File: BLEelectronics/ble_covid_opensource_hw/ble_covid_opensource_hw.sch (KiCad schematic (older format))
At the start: 35 parts, among them IC1 LTC4412xS6, IC2 LTC4054LES5-4.2#TRPBF, IC3 PCF8523T, IC4 MX25R6435FM2IL0, J1 USB_B_Micro, J2 Conn_01x01_Female, Q1 Si2307CDS, U1 BAT-HLD-001, U2 ESD401, U3 ESD401, U4 LP5907MFX-3.3

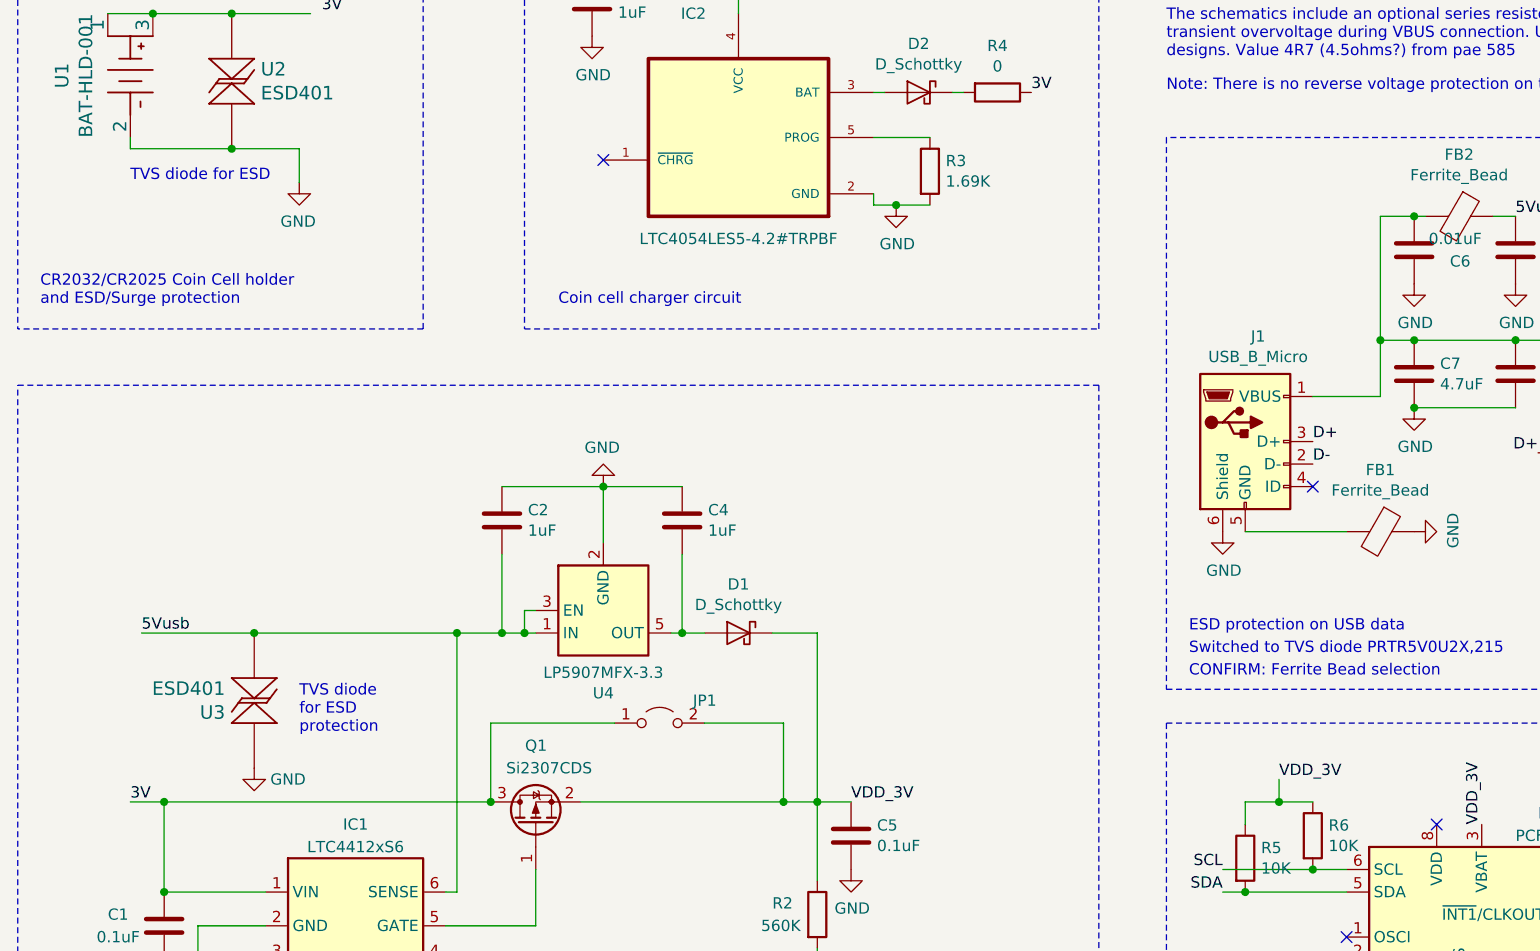
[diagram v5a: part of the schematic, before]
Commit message: hw mvp 1b all components on PCB, todo: traces.
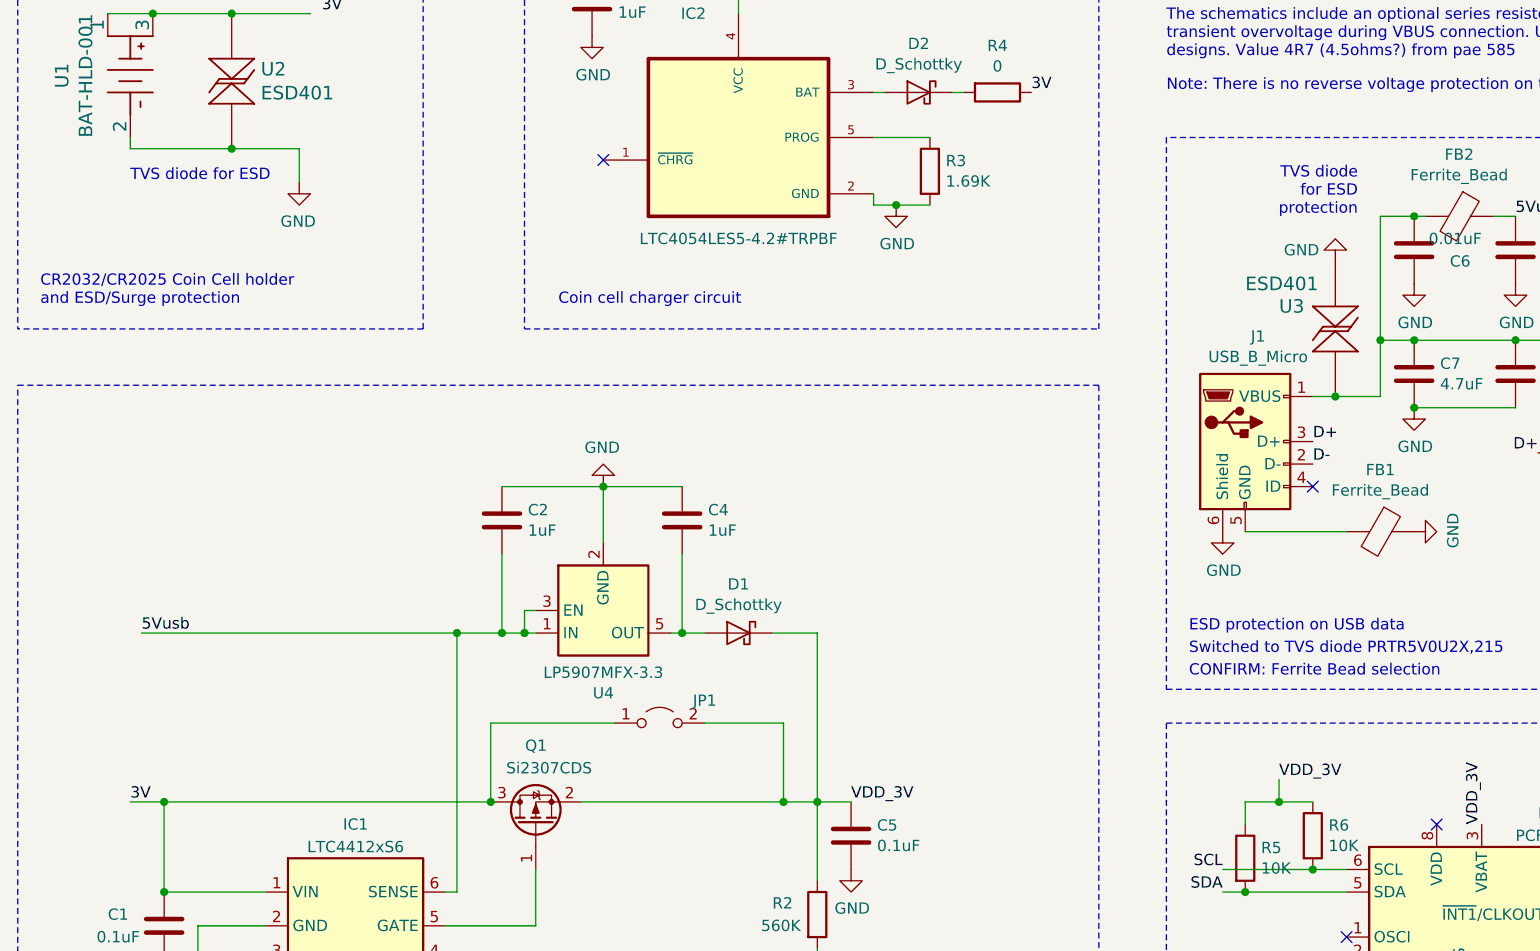
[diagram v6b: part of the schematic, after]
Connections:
- net 5Vusb: no longer U3.1
- net at C6.2, C7.1, C9.2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: now also U3.1
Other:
- moved on the sheet: U3
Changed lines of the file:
@@
 	3150 5100 1700 5100
-Wire Wire Line
-	2100 4350 3000 4350
 Wire Wire Line
 	3000 4350 3200 4350
@@
 	1    0    0    -1
 $EndComp
-$Comp
-L power:GND #PWR02
-U 1 1 5EA2FE2A
-P 2100 4950
-F 0 "#PWR02" H 2100 4700 50  0001 C CNN
-F 1 "GND" H 2250 4900 50  0000 C CNN
-F 2 "" H 2100 4950 50  0001 C CNN
-F 3 "" H 2100 4950 50  0001 C CNN
-	1    2100 4950
-	1    0    0    -1
-$EndComp
 Text Label 1600 4350 0    50   ~ 0
 5Vusb
-Text Notes 2300 4800 0    50   ~ 0
+Text Notes 7000 2500 2    50   ~ 0
 TVS diode \nfor ESD\nprotection
 Wire Wire Line
@@
 Wire Wire Line
 	1700 5800 1850 5800
-Wire Wire Line
-	1600 4350 2100 4350
 Connection ~ 3300 4350
 Connection ~ 3200 4350
 Connection ~ 4000 4350
 Connection ~ 1700 5800
-$Comp
-L ESD401DPYR:ESD401DPYR U3
-U 1 1 5EA4E7E7
-P 2100 4650
-F 0 "U3" V 2153 4521 60  0000 R CNN
-F 1 "ESD401" V 2047 4521 60  0000 R CNN
-F 2 "0my_footprints:ESD401DPYR" H 2100 4590 60  0001 C CNN
-F 3 "http://www.ti.com/general/docs/suppproductinfo.tsp?distId=10&gotoUrl=http%3A%2F%2Fwww.ti.com%2Flit%2Fgpn%2Fesd401" V 1994 4521 60  0001 R CNN
-F 4 "Texas Instruments" H -250 2650 50  0001 C CNN "MFR"
-F 5 "ESD401DPYR" H -250 2650 50  0001 C CNN "MPN"
-F 6 "296-47160-1-ND" H -250 2650 50  0001 C CNN "DPN"
-F 7 "-" H -250 2650 50  0001 C CNN "LCSCPN"
-F 8 "-" H -250 2650 50  0001 C CNN "SPR"
-F 9 "-" H -250 2650 50  0001 C CNN "SPN"
-F 10 "-" H -250 2650 50  0001 C CNN "SIM"
-	1    2100 4650
-	0    1    1    0
-$EndComp
-Connection ~ 2100 4350
-Wire Wire Line
-	7100 3300 6800 3300
+Wire Wire Line
+	7100 3300 6900 3300
 Wire Notes Line
 	8450 6450 8450 4750
@@
 Text Notes 6150 1950 0    50   ~ 0
 Note: There is no reverse voltage protection on the power connections. (pg 14 Dongle guide)
+$Comp
+L ESD401DPYR:ESD401DPYR U3
+U 1 1 5EA4E7E7
+P 6900 3000
+F 0 "U3" V 7000 3250 60  0000 R CNN
+F 1 "ESD401" V 7100 3400 60  0000 R CNN
+F 2 "0my_footprints:ESD401DPYR" H 6900 2940 60  0001 C CNN
+F 3 "http://www.ti.com/general/docs/suppproductinfo.tsp?distId=10&gotoUrl=http%3A%2F%2Fwww.ti.com%2Flit%2Fgpn%2Fesd401" V 6794 2871 60  0001 R CNN
+F 4 "Texas Instruments" H 4550 1000 50  0001 C CNN "MFR"
+F 5 "ESD401DPYR" H 4550 1000 50  0001 C CNN "MPN"
+F 6 "296-47160-1-ND" H 4550 1000 50  0001 C CNN "DPN"
+F 7 "-" H 4550 1000 50  0001 C CNN "LCSCPN"
+F 8 "-" H 4550 1000 50  0001 C CNN "SPR"
+F 9 "-" H 4550 1000 50  0001 C CNN "SPN"
+F 10 "-" H 4550 1000 50  0001 C CNN "SIM"
+	1    6900 3000
+	0    -1   -1   0
+$EndComp
+$Comp
+L power:GND #PWR02
+U 1 1 5EA2FE2A
+P 6900 2700
+F 0 "#PWR02" H 6900 2450 50  0001 C CNN
+F 1 "GND" H 7050 2650 50  0000 C CNN
+F 2 "" H 6900 2700 50  0001 C CNN
+F 3 "" H 6900 2700 50  0001 C CNN
+	1    6900 2700
+	-1   0    0    1
+$EndComp
+Connection ~ 6900 3300
+Wire Wire Line
+	6900 3300 6800 3300
+Wire Wire Line
+	1600 4350 3000 4350
 $EndSCHEMATC

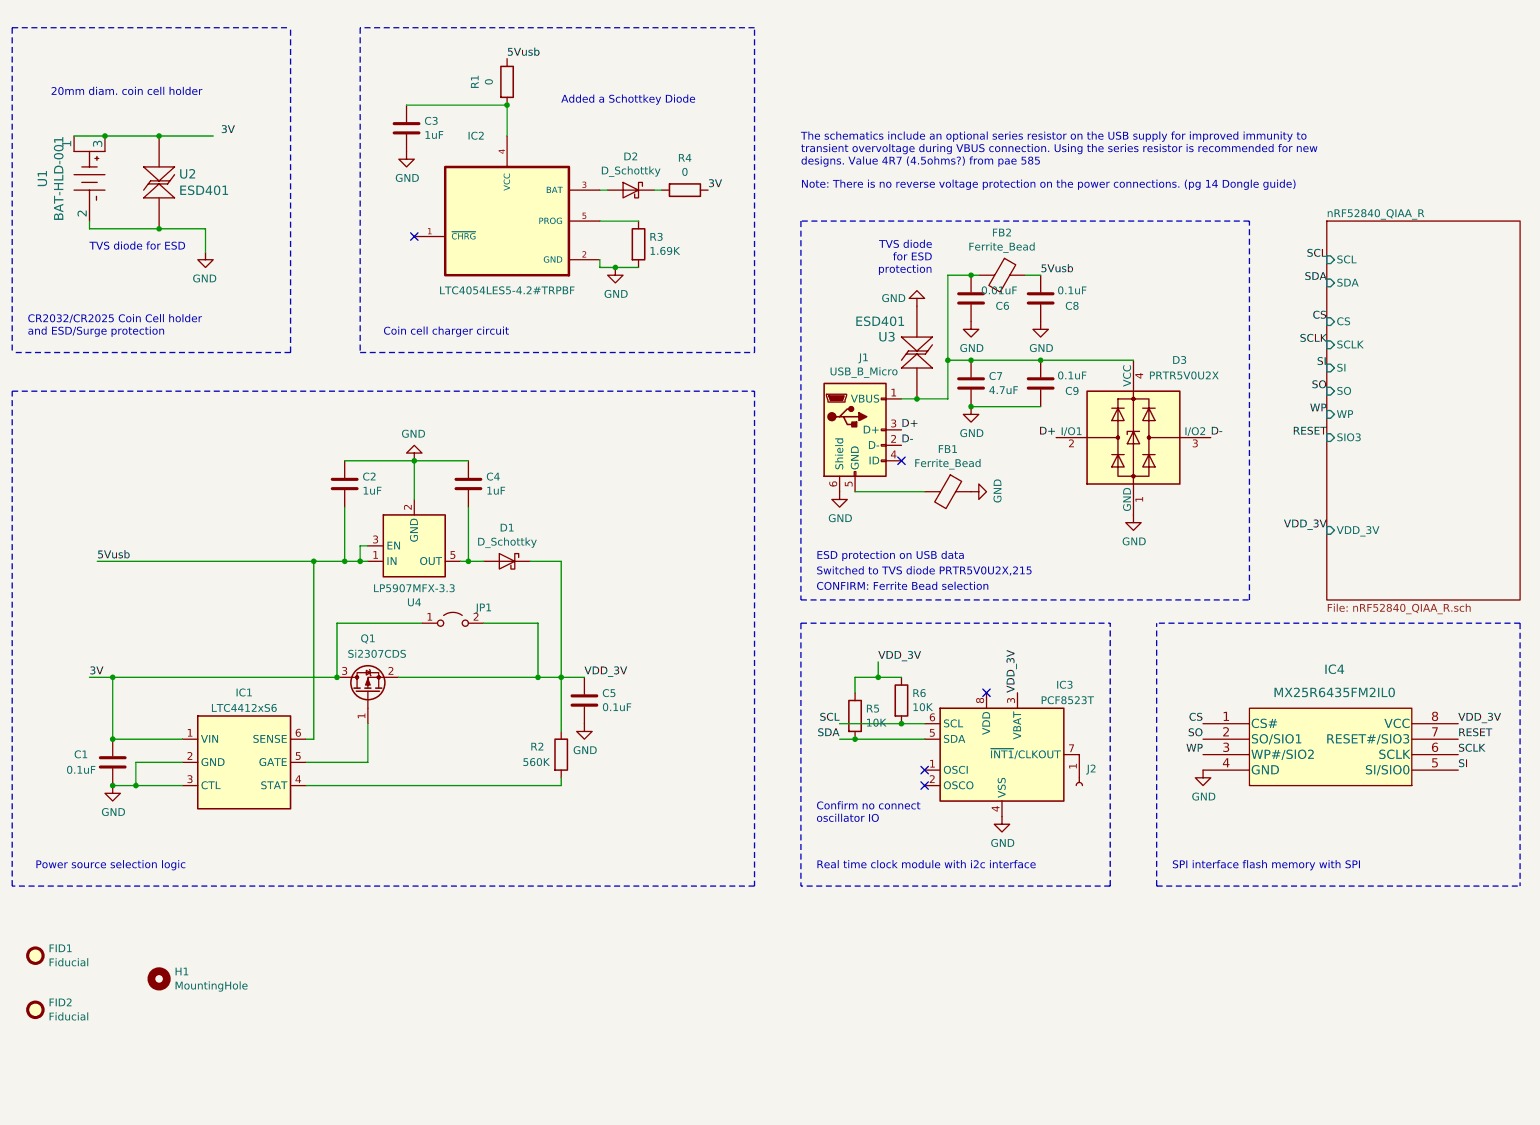
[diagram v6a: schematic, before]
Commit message: schematic updated to be close to the Dongle. Layout update to closer to final footprint. Some traces todo.
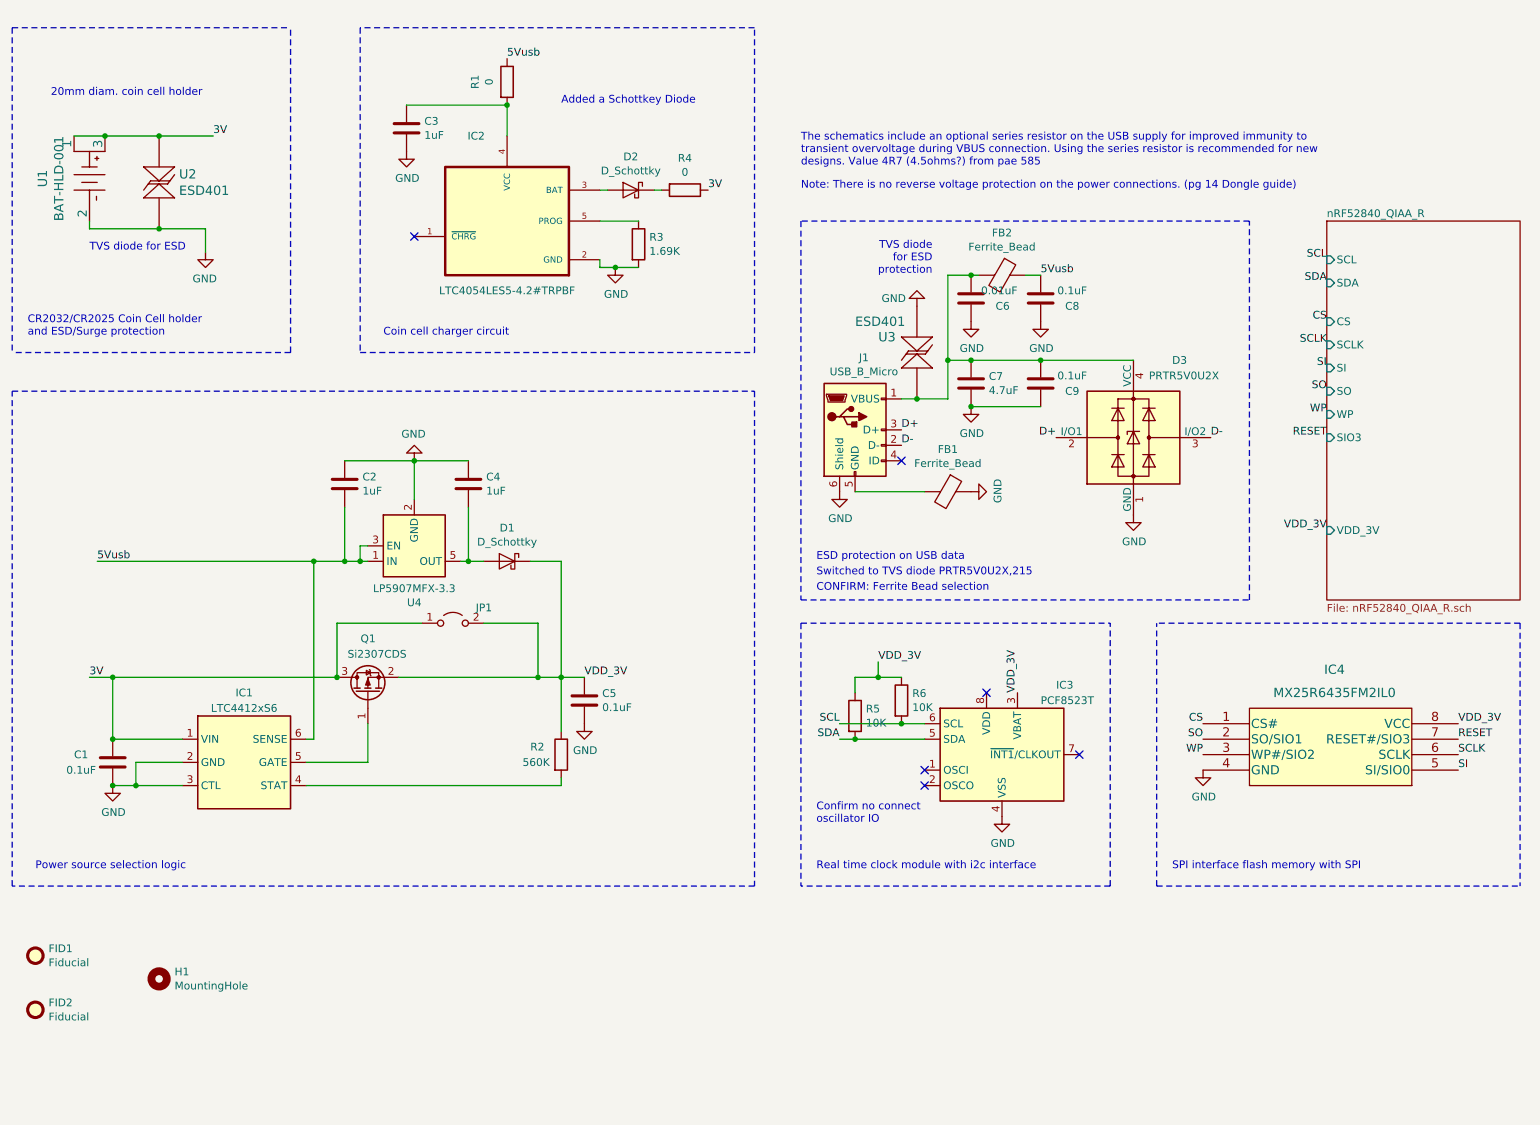
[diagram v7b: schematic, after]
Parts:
- removed J2: Conn_01x01_Female, Connector_PinHeader_2.54mm:PinHeader_1x01_P2.54mm_Vertical, symbol Connector:Conn_01x01_Female
- H1: footprint MountingHole:MountingHole_2.2mm_M2_Pad -> MountingHole:MountingHole_2.2mm_M2_DIN965_Pad
- R4: footprint Resistor_SMD:R_0603_1608Metric_Pad1.05x0.95mm_HandSolder -> Resistor_SMD:R_0402_1005Metric
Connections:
- net 3V: now also U1.1, U1.3, U2.2
- no-connect marks 5 -> 6
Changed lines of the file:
@@
 F 0 "R4" V 5193 1950 50  0000 C CNN
 F 1 "0" V 5284 1950 50  0000 C CNN
-F 2 "Resistor_SMD:R_0603_1608Metric_Pad1.05x0.95mm_HandSolder" V 5330 1950 50  0001 C CNN
+F 2 "Resistor_SMD:R_0402_1005Metric" V 5330 1950 50  0001 C CNN
 F 3 "https://www.yageo.com/upload/media/product/productsearch/datasheet/rchip/PYu-RC_Group_51_RoHS_L_10.pdf" H 5400 1950 50  0001 C CNN
 F 4 "RC0603JR-070RL" V 5400 1950 50  0001 C CNN "MPN"
@@
 F 0 "H1" H 2100 7096 50  0000 L CNN
 F 1 "MountingHole" H 2100 7005 50  0000 L CNN
-F 2 "MountingHole:MountingHole_2.2mm_M2_Pad" H 2000 7050 50  0001 C CNN
+F 2 "MountingHole:MountingHole_2.2mm_M2_DIN965_Pad" H 2000 7050 50  0001 C CNN
 F 3 "~" H 2000 7050 50  0001 C CNN
 F 4 "-" H 0   0   50  0001 C CNN "MFR"
@@
 $EndComp
 $Comp
-L Connector:Conn_01x01_Female J2
-U 1 1 5EA8C546
-P 7950 5800
-F 0 "J2" V 7842 5848 50  0000 L CNN
-F 1 "Conn_01x01_Female" H 7978 5735 50  0001 L CNN
-F 2 "Connector_PinHeader_2.54mm:PinHeader_1x01_P2.54mm_Vertical" H 7950 5800 50  0001 C CNN
-F 3 "~" H 7950 5800 50  0001 C CNN
-F 4 "-" H 0   1450 50  0001 C CNN "MFR"
-F 5 "-" H 0   1450 50  0001 C CNN "MPN"
-F 6 "-" H 0   1450 50  0001 C CNN "DPN"
-F 7 "-" H 0   1450 50  0001 C CNN "LCSCPN"
-F 8 "-" H 0   1450 50  0001 C CNN "SPR"
-F 9 "-" H 0   1450 50  0001 C CNN "SPN"
-F 10 "-" H 0   1450 50  0001 C CNN "SIM"
-	1    7950 5800
-	0    1    1    0
-$EndComp
-$Comp
 L ESD401DPYR:ESD401DPYR U2
 U 1 1 5EA48F38
@@
 Text Label 4250 1100 0    50   ~ 0
 5Vusb
-Text Label 5550 1950 0    50   ~ 0
-3V
 Text Notes 3450 2900 0    50   ~ 0
 Coin cell charger circuit
 Text Notes 1150 2900 0    50   ~ 0
 CR2032/CR2025 Coin Cell holder \nand ESD/Surge protection
-Text Label 2400 1600 0    50   ~ 0
+Text Label 2350 1600 0    50   ~ 0
 3V
 Text Notes 8550 6350 0    50   ~ 0
@@
 Wire Wire Line
 	1600 4350 3000 4350
+NoConn ~ 7950 5600
+Text Label 5550 1950 0    50   ~ 0
+3V
 $EndSCHEMATC

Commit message: hw mvp 1b layout full draft. Antenna still throwing DRC errors to be checked.
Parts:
- added FID3: Fiducial, Fiducial:Fiducial_0.5mm_Mask1mm, symbol Mechanical:Fiducial
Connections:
- net RESET renamed SIO3
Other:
- moved on the sheet: FID2
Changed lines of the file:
@@
 L Mechanical:Fiducial FID2
 U 1 1 5E9C7A0B
-P 1200 7250
-F 0 "FID2" H 1285 7296 50  0000 L CNN
-F 1 "Fiducial" H 1285 7205 50  0000 L CNN
-F 2 "Fiducial:Fiducial_0.5mm_Mask1mm" H 1200 7250 50  0001 C CNN
-F 3 "~" H 1200 7250 50  0001 C CNN
-F 4 "-" H 0   0   50  0001 C CNN "MFR"
-F 5 "-" H 0   0   50  0001 C CNN "MPN"
-F 6 "-" H 0   0   50  0001 C CNN "DPN"
-F 7 "-" H 0   0   50  0001 C CNN "LCSCPN"
-F 8 "-" H 0   0   50  0001 C CNN "SPR"
-F 9 "-" H 0   0   50  0001 C CNN "SPN"
-F 10 "-" H 0   0   50  0001 C CNN "SIM"
-	1    1200 7250
+P 1200 7200
+F 0 "FID2" H 1285 7246 50  0000 L CNN
+F 1 "Fiducial" H 1285 7155 50  0000 L CNN
+F 2 "Fiducial:Fiducial_0.5mm_Mask1mm" H 1200 7200 50  0001 C CNN
+F 3 "~" H 1200 7200 50  0001 C CNN
+F 4 "-" H 0   -50 50  0001 C CNN "MFR"
+F 5 "-" H 0   -50 50  0001 C CNN "MPN"
+F 6 "-" H 0   -50 50  0001 C CNN "DPN"
+F 7 "-" H 0   -50 50  0001 C CNN "LCSCPN"
+F 8 "-" H 0   -50 50  0001 C CNN "SPR"
+F 9 "-" H 0   -50 50  0001 C CNN "SPN"
+F 10 "-" H 0   -50 50  0001 C CNN "SIM"
+	1    1200 7200
 	1    0    0    -1
 $EndComp
@@
 SO
 Text Label 10400 5500 0    50   ~ 0
-RESET
+SIO3
 Text Label 8750 5400 2    50   ~ 0
 CS
@@
 Text Label 9550 4150 2    50   ~ 0
 VDD_3V
-Text Label 9550 3550 2    50   ~ 0
-RESET
 Text Label 9550 2950 2    50   ~ 0
 SCLK
@@
 Text Label 5550 1950 0    50   ~ 0
 3V
+$Comp
+L Mechanical:Fiducial FID3
+U 1 1 5EAF7822
+P 1200 7500
+F 0 "FID3" H 1285 7546 50  0000 L CNN
+F 1 "Fiducial" H 1285 7455 50  0000 L CNN
+F 2 "Fiducial:Fiducial_0.5mm_Mask1mm" H 1200 7500 50  0001 C CNN
+F 3 "~" H 1200 7500 50  0001 C CNN
+F 4 "-" H 0   250 50  0001 C CNN "MFR"
+F 5 "-" H 0   250 50  0001 C CNN "MPN"
+F 6 "-" H 0   250 50  0001 C CNN "DPN"
+F 7 "-" H 0   250 50  0001 C CNN "LCSCPN"
+F 8 "-" H 0   250 50  0001 C CNN "SPR"
+F 9 "-" H 0   250 50  0001 C CNN "SPN"
+F 10 "-" H 0   250 50  0001 C CNN "SIM"
+	1    1200 7500
+	1    0    0    -1
+$EndComp
+Text Label 9550 3550 2    50   ~ 0
+SIO3
 $EndSCHEMATC
